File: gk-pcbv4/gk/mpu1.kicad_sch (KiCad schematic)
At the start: 43 parts, among them U5 STM32MP255DAI3

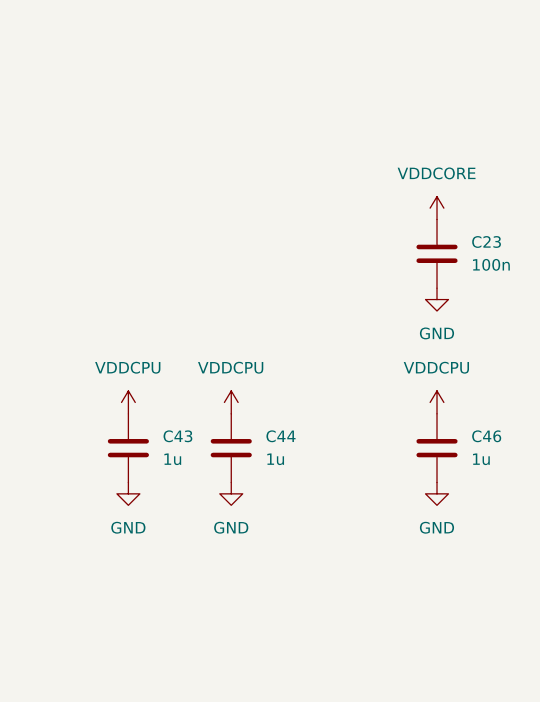
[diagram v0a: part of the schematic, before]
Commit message: update silkscreen text
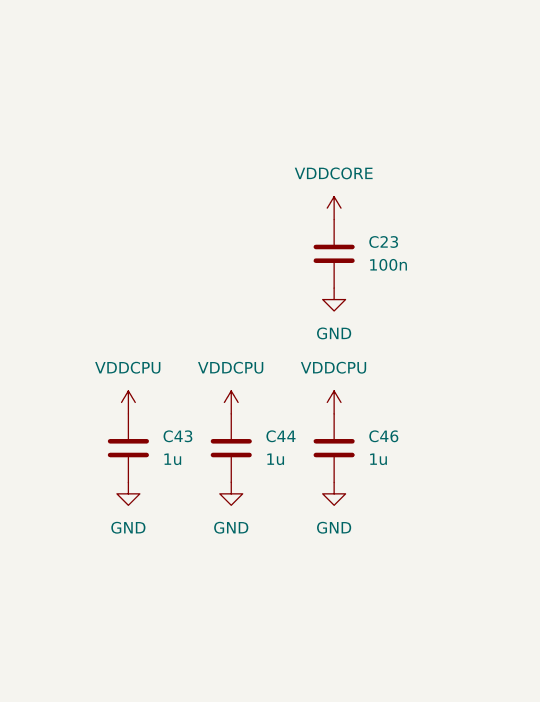
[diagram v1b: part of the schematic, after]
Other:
- moved on the sheet: C23, C46
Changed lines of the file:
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@@
 	(symbol
 		(lib_id "power:VDD")
-		(at 279.4 121.92 0)
+		(at 267.97 121.92 0)
 		(unit 1)
 		(exclude_from_sim no)
@@
 		(fields_autoplaced yes)
 		(property "Reference" "#PWR098"
-			(at 279.4 125.73 0)
+			(at 267.97 125.73 0)
 			(effects
 				(font
@@
 		)
 		(property "Value" "VDDCORE"
-			(at 279.4 116.84 0)
+			(at 267.97 116.84 0)
 			(effects
 				(font
@@
 		)
 		(property "Footprint" ""
-			(at 279.4 121.92 0)
+			(at 267.97 121.92 0)
 			(effects
 				(font
@@
 		)
 		(property "Datasheet" ""
-			(at 279.4 121.92 0)
+			(at 267.97 121.92 0)
 			(effects
 				(font
@@
 		)
 		(property "Description" "Power symbol creates a global label with name \"VDD\""
-			(at 279.4 121.92 0)
+			(at 267.97 121.92 0)
 			(effects
 				(font
@@
 	(symbol
 		(lib_id "Device:C")
-		(at 279.4 125.73 0)
+		(at 267.97 125.73 0)
 		(unit 1)
 		(exclude_from_sim no)
@@
 		(fields_autoplaced yes)
 		(property "Reference" "C23"
-			(at 283.21 124.4599 0)
+			(at 271.78 124.4599 0)
 			(effects
 				(font
@@
 		)
 		(property "Value" "100n"
-			(at 283.21 126.9999 0)
+			(at 271.78 126.9999 0)
 			(effects
 				(font
@@
 		)
 		(property "Footprint" "Capacitor_SMD:C_0402_1005Metric"
-			(at 280.3652 129.54 0)
+			(at 268.9352 129.54 0)
 			(effects
 				(font
@@
 		)
 		(property "Datasheet" "~"
-			(at 279.4 125.73 0)
+			(at 267.97 125.73 0)
 			(effects
 				(font
@@
 		)
 		(property "Description" "Unpolarized capacitor"
-			(at 279.4 125.73 0)
+			(at 267.97 125.73 0)
 			(effects
 				(font
@@
 	(symbol
 		(lib_id "power:GND")
-		(at 279.4 129.54 0)
+		(at 267.97 129.54 0)
 		(unit 1)
 		(exclude_from_sim no)
@@
 		(fields_autoplaced yes)
 		(property "Reference" "#PWR0110"
-			(at 279.4 135.89 0)
+			(at 267.97 135.89 0)
 			(effects
 				(font
@@
 		)
 		(property "Value" "GND"
-			(at 279.4 134.62 0)
+			(at 267.97 134.62 0)
 			(effects
 				(font
@@
 		)
 		(property "Footprint" ""
-			(at 279.4 129.54 0)
+			(at 267.97 129.54 0)
 			(effects
 				(font
@@
 		)
 		(property "Datasheet" ""
-			(at 279.4 129.54 0)
+			(at 267.97 129.54 0)
 			(effects
 				(font
@@
 		)
 		(property "Description" "Power symbol creates a global label with name \"GND\" , ground"
-			(at 279.4 129.54 0)
+			(at 267.97 129.54 0)
 			(effects
 				(font
@@
 	(symbol
 		(lib_id "power:GND")
-		(at 279.4 151.13 0)
+		(at 267.97 151.13 0)
 		(unit 1)
 		(exclude_from_sim no)
@@
 		(fields_autoplaced yes)
 		(property "Reference" "#PWR0156"
-			(at 279.4 157.48 0)
+			(at 267.97 157.48 0)
 			(effects
 				(font
@@
 		)
 		(property "Value" "GND"
-			(at 279.4 156.21 0)
+			(at 267.97 156.21 0)
 			(effects
 				(font
@@
 		)
 		(property "Footprint" ""
-			(at 279.4 151.13 0)
+			(at 267.97 151.13 0)
 			(effects
 				(font
@@
 		)
 		(property "Datasheet" ""
-			(at 279.4 151.13 0)
+			(at 267.97 151.13 0)
 			(effects
 				(font
@@
 		)
 		(property "Description" "Power symbol creates a global label with name \"GND\" , ground"
-			(at 279.4 151.13 0)
+			(at 267.97 151.13 0)
 			(effects
 				(font
@@
 	(symbol
 		(lib_id "Device:C")
-		(at 279.4 147.32 0)
+		(at 267.97 147.32 0)
 		(unit 1)
 		(exclude_from_sim no)
@@
 		(fields_autoplaced yes)
 		(property "Reference" "C46"
-			(at 283.21 146.0499 0)
+			(at 271.78 146.0499 0)
 			(effects
 				(font
@@
 		)
 		(property "Value" "1u"
-			(at 283.21 148.5899 0)
+			(at 271.78 148.5899 0)
 			(effects
 				(font
@@
 		)
 		(property "Footprint" "Capacitor_SMD:C_0402_1005Metric"
-			(at 280.3652 151.13 0)
+			(at 268.9352 151.13 0)
 			(effects
 				(font
@@
 		)
 		(property "Datasheet" "~"
-			(at 279.4 147.32 0)
+			(at 267.97 147.32 0)
 			(effects
 				(font
@@
 		)
 		(property "Description" "Unpolarized capacitor"
-			(at 279.4 147.32 0)
+			(at 267.97 147.32 0)
 			(effects
 				(font
@@
 	(symbol
 		(lib_id "power:VDD")
-		(at 279.4 143.51 0)
+		(at 267.97 143.51 0)
 		(unit 1)
 		(exclude_from_sim no)
@@
 		(fields_autoplaced yes)
 		(property "Reference" "#PWR0133"
-			(at 279.4 147.32 0)
+			(at 267.97 147.32 0)
 			(effects
 				(font
@@
 		)
 		(property "Value" "VDDCPU"
-			(at 279.4 138.43 0)
+			(at 267.97 138.43 0)
 			(effects
 				(font
@@
 		)
 		(property "Footprint" ""
-			(at 279.4 143.51 0)
+			(at 267.97 143.51 0)
 			(effects
 				(font
@@
 		)
 		(property "Datasheet" ""
-			(at 279.4 143.51 0)
+			(at 267.97 143.51 0)
 			(effects
 				(font
@@
 		)
 		(property "Description" "Power symbol creates a global label with name \"VDD\""
-			(at 279.4 143.51 0)
+			(at 267.97 143.51 0)
 			(effects
 				(font

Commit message: update pin name
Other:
- note added: "VDDGPU"
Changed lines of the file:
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@@
 	(generator_version "9.0")
 	(paper "A4")
+	(text "VDDGPU"
+		(exclude_from_sim no)
+		(at 187.452 85.598 90)
+		(effects
+			(font
+				(size 1.27 1.27)
+			)
+			(justify left)
+		)
+	)
 	(junction
 		(at 148.59 27.94)
@@
 		)
 		(stroke
+			(width 0)
+			(type default)
+		)
+	)
+	(polyline
+		(pts
+			(xy 189.23 76.835) (xy 189.23 86.36)
+		)
+		(stroke
